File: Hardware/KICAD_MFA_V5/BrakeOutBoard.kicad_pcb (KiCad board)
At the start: 2 copper layers, 63 x 80 mm, 65 parts, among them J1 Conn_01x19_Socket, J2 Conn_01x19_Socket, K15 K15, K3 K31, K30 K30, Q1 LBSS84LT1G, Q2 MMDT3904, U1 LTV-847, U2 LTV-847, U3 LTV-847, U4 EL817(B)-F, U5 SN65HVD230DR, U6 MCP23017_ML

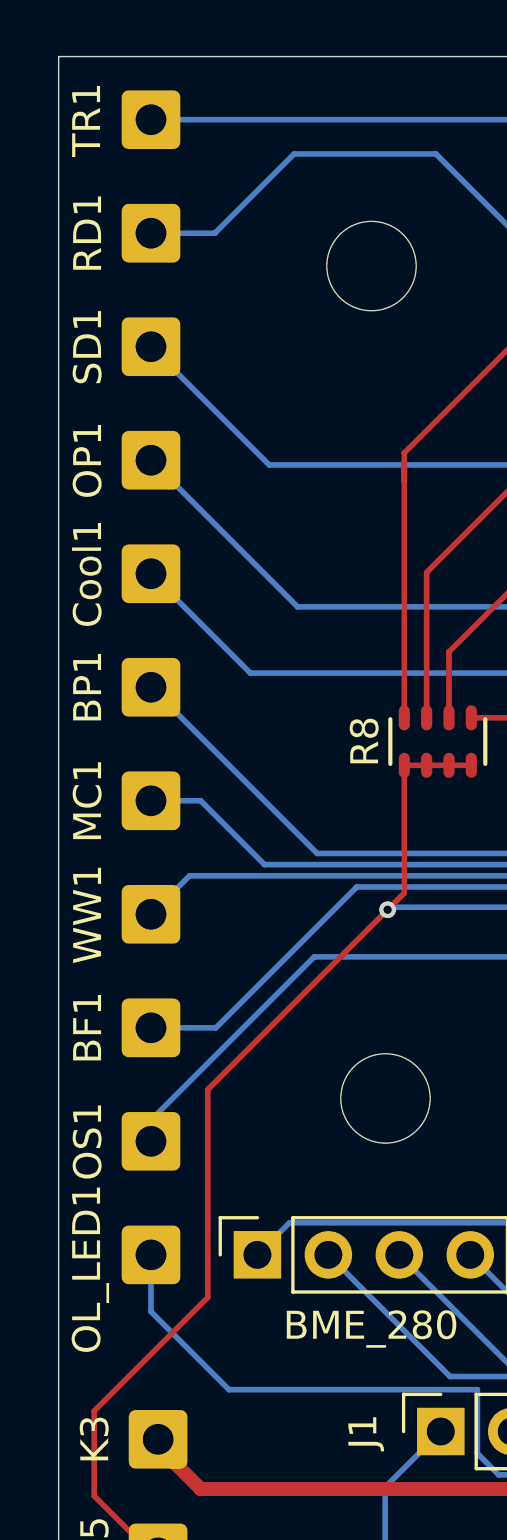
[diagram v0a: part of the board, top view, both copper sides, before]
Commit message: Added some DEBUG Statements and Shutdown Time is now a defined number so it can be changed easy.
Signed-off-by: Norbert Schechner <nieson@web.de>
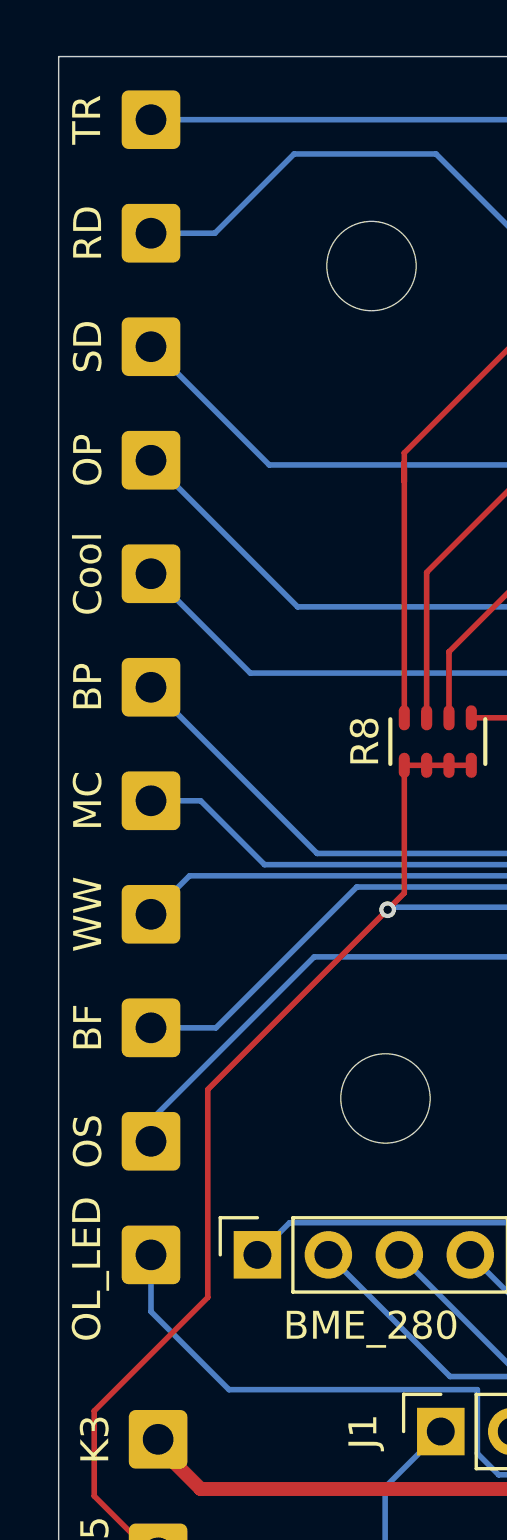
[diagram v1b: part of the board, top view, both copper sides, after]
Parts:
- renumbered BF1 to BF, BP1 to BP, Cool1 to Cool, MC1 to MC, OL_LED1 to OL_LED, OP1 to OP, OS1 to OS, RD1 to RD, SD1 to SD, TR1 to TR, WW1 to WW
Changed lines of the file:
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@@
 		(descr "Soldered wire connection, for a single 0.5 mm² wire, basic insulation, conductor diameter 0.9mm, outer diameter 2.1mm, size source Multi-Contact FLEXI-E 0.5 (https://ec.staubli.com/AcroFiles/Catalogues/TM_Cab-Main-11014119_(en)_hi.pdf), bend radius 3 times outer diameter, generated with kicad-footprint-generator")
 		(tags "connector wire 0.5sqmm")
-		(property "Reference" "BF1"
+		(property "Reference" "BF"
 			(at 0 -2.25 90)
 			(layer "F.SilkS")
@@
 		(descr "Soldered wire connection, for a single 0.5 mm² wire, basic insulation, conductor diameter 0.9mm, outer diameter 2.1mm, size source Multi-Contact FLEXI-E 0.5 (https://ec.staubli.com/AcroFiles/Catalogues/TM_Cab-Main-11014119_(en)_hi.pdf), bend radius 3 times outer diameter, generated with kicad-footprint-generator")
 		(tags "connector wire 0.5sqmm")
-		(property "Reference" "MC1"
+		(property "Reference" "MC"
 			(at 0 -2.25 90)
 			(layer "F.SilkS")
@@
 		(descr "Soldered wire connection, for a single 0.5 mm² wire, basic insulation, conductor diameter 0.9mm, outer diameter 2.1mm, size source Multi-Contact FLEXI-E 0.5 (https://ec.staubli.com/AcroFiles/Catalogues/TM_Cab-Main-11014119_(en)_hi.pdf), bend radius 3 times outer diameter, generated with kicad-footprint-generator")
 		(tags "connector wire 0.5sqmm")
-		(property "Reference" "WW1"
+		(property "Reference" "WW"
 			(at 0 -2.25 90)
 			(layer "F.SilkS")
@@
 		(descr "Soldered wire connection, for a single 0.5 mm² wire, basic insulation, conductor diameter 0.9mm, outer diameter 2.1mm, size source Multi-Contact FLEXI-E 0.5 (https://ec.staubli.com/AcroFiles/Catalogues/TM_Cab-Main-11014119_(en)_hi.pdf), bend radius 3 times outer diameter, generated with kicad-footprint-generator")
 		(tags "connector wire 0.5sqmm")
-		(property "Reference" "SD1"
+		(property "Reference" "SD"
 			(at 0 -2.25 90)
 			(layer "F.SilkS")
@@
 		(descr "Soldered wire connection, for a single 0.5 mm² wire, basic insulation, conductor diameter 0.9mm, outer diameter 2.1mm, size source Multi-Contact FLEXI-E 0.5 (https://ec.staubli.com/AcroFiles/Catalogues/TM_Cab-Main-11014119_(en)_hi.pdf), bend radius 3 times outer diameter, generated with kicad-footprint-generator")
 		(tags "connector wire 0.5sqmm")
-		(property "Reference" "OP1"
+		(property "Reference" "OP"
 			(at 0 -2.25 90)
 			(layer "F.SilkS")
@@
 		(descr "Soldered wire connection, for a single 0.5 mm² wire, basic insulation, conductor diameter 0.9mm, outer diameter 2.1mm, size source Multi-Contact FLEXI-E 0.5 (https://ec.staubli.com/AcroFiles/Catalogues/TM_Cab-Main-11014119_(en)_hi.pdf), bend radius 3 times outer diameter, generated with kicad-footprint-generator")
 		(tags "connector wire 0.5sqmm")
-		(property "Reference" "RD1"
+		(property "Reference" "RD"
 			(at 0 -2.25 90)
 			(layer "F.SilkS")
@@
 		(descr "Soldered wire connection, for a single 0.5 mm² wire, basic insulation, conductor diameter 0.9mm, outer diameter 2.1mm, size source Multi-Contact FLEXI-E 0.5 (https://ec.staubli.com/AcroFiles/Catalogues/TM_Cab-Main-11014119_(en)_hi.pdf), bend radius 3 times outer diameter, generated with kicad-footprint-generator")
 		(tags "connector wire 0.5sqmm")
-		(property "Reference" "BP1"
+		(property "Reference" "BP"
 			(at 0 -2.25 90)
 			(layer "F.SilkS")
@@
 		(descr "Soldered wire connection, for a single 0.5 mm² wire, basic insulation, conductor diameter 0.9mm, outer diameter 2.1mm, size source Multi-Contact FLEXI-E 0.5 (https://ec.staubli.com/AcroFiles/Catalogues/TM_Cab-Main-11014119_(en)_hi.pdf), bend radius 3 times outer diameter, generated with kicad-footprint-generator")
 		(tags "connector wire 0.5sqmm")
-		(property "Reference" "OL_LED1"
+		(property "Reference" "OL_LED"
 			(at -0.508 -2.286 90)
 			(layer "F.SilkS")
@@
 		(descr "Soldered wire connection, for a single 0.5 mm² wire, basic insulation, conductor diameter 0.9mm, outer diameter 2.1mm, size source Multi-Contact FLEXI-E 0.5 (https://ec.staubli.com/AcroFiles/Catalogues/TM_Cab-Main-11014119_(en)_hi.pdf), bend radius 3 times outer diameter, generated with kicad-footprint-generator")
 		(tags "connector wire 0.5sqmm")
-		(property "Reference" "OS1"
+		(property "Reference" "OS"
 			(at 0 -2.25 90)
 			(layer "F.SilkS")
@@
 		(descr "Soldered wire connection, for a single 0.5 mm² wire, basic insulation, conductor diameter 0.9mm, outer diameter 2.1mm, size source Multi-Contact FLEXI-E 0.5 (https://ec.staubli.com/AcroFiles/Catalogues/TM_Cab-Main-11014119_(en)_hi.pdf), bend radius 3 times outer diameter, generated with kicad-footprint-generator")
 		(tags "connector wire 0.5sqmm")
-		(property "Reference" "Cool1"
+		(property "Reference" "Cool"
 			(at 0 -2.25 90)
 			(layer "F.SilkS")
@@
 		(descr "Soldered wire connection, for a single 0.5 mm² wire, basic insulation, conductor diameter 0.9mm, outer diameter 2.1mm, size source Multi-Contact FLEXI-E 0.5 (https://ec.staubli.com/AcroFiles/Catalogues/TM_Cab-Main-11014119_(en)_hi.pdf), bend radius 3 times outer diameter, generated with kicad-footprint-generator")
 		(tags "connector wire 0.5sqmm")
-		(property "Reference" "TR1"
+		(property "Reference" "TR"
 			(at 0 2.286 90)
 			(layer "F.SilkS")
